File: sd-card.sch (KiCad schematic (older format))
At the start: 11 parts, among them J6 Micro_SD_Card_Det, U8 SN74AHC1G125DBVR

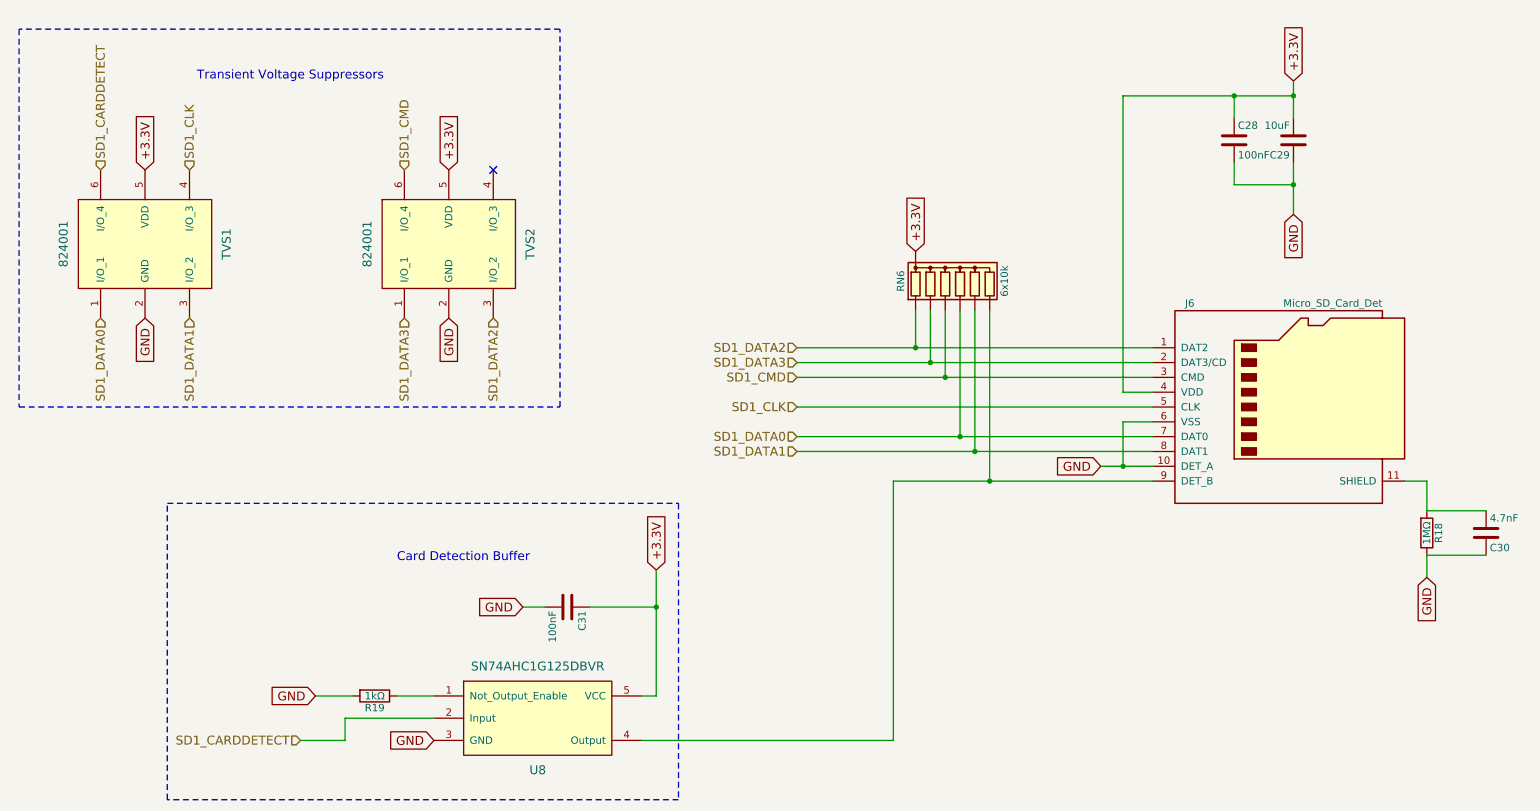
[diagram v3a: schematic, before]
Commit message: I have verified the schematic a second time (except the so-dimm), and I have selected all of the components with links and footprint. I need to verify the schematic a third time and root
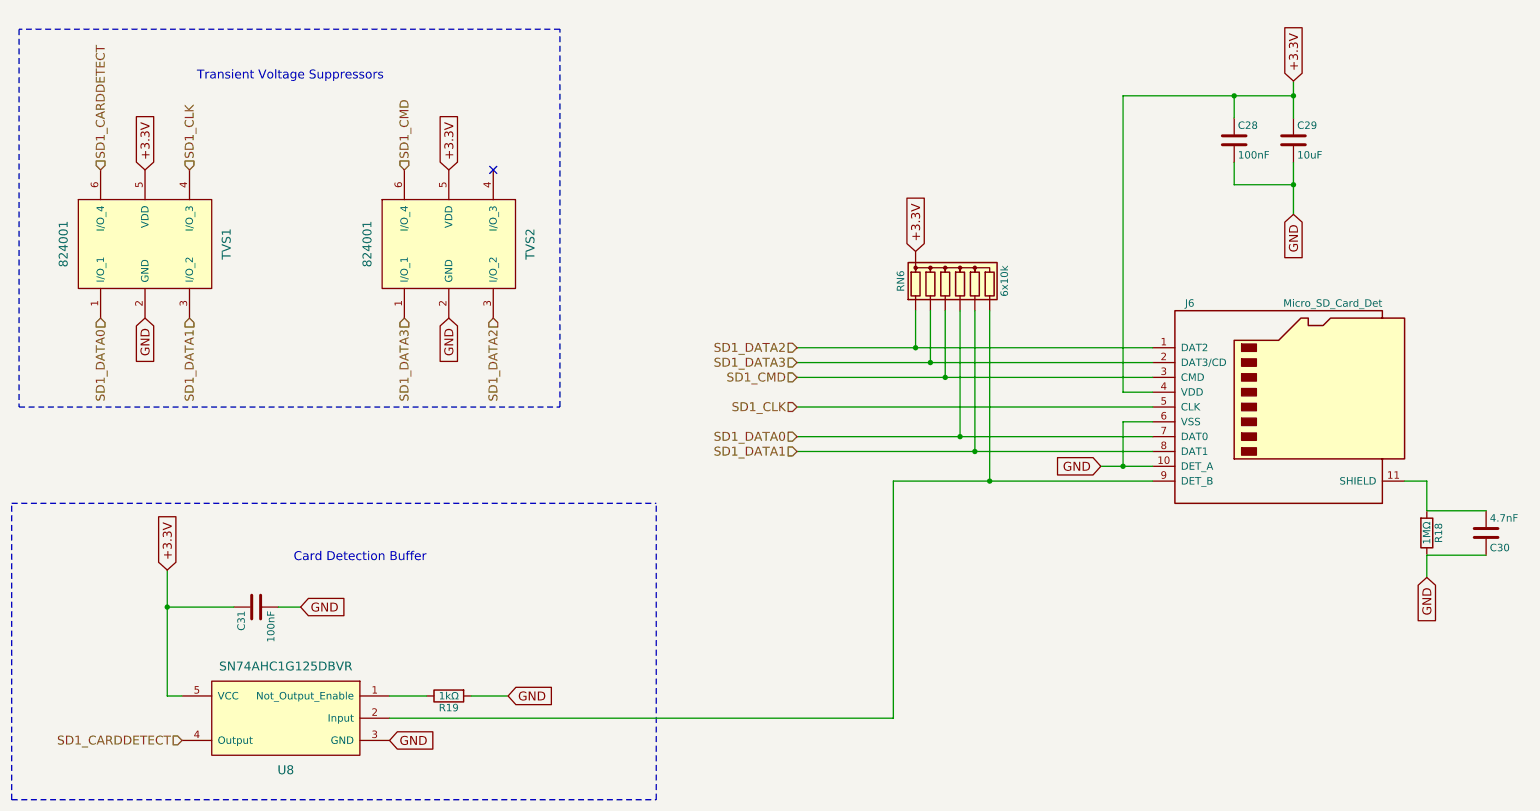
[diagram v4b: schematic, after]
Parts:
- RN6: footprint Resistors_THT:R_Array_SIP7 -> water:YC158-Yageo-Handsoldering
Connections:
- net +3.3V: now also C29.1; no longer C29.2
- net GND: now also C29.2; no longer C29.1
- net SD1_CARDDETECT: now also U8.4 (Output); no longer U8.2 (Input)
- net at J6.9 (DET_B), RN6.7 (R6): now also U8.2 (Input); no longer U8.4 (Output)
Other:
- moved on the sheet: C31, R19, U8
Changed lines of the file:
@@
 Text HLabel 6250 3300 0    60   Input ~ 0
 SD1_CLK
-Text HLabel 2900 5550 0    60   Input ~ 0
+Text HLabel 2100 5550 0    60   Input ~ 0
 SD1_CARDDETECT
 Text GLabel 7050 2250 1    60   Input ~ 0
@@
 F 0 "RN6" V 6950 2450 50  0000 C CNN
 F 1 "6x10k" V 7650 2450 50  0000 C CNN
-F 2 "Resistors_THT:R_Array_SIP7" V 7725 2450 50  0001 C CNN
-F 3 "http://hu.farnell.com/bourns/cay17-103jalf/resistor-n-w-8res-10kohm-5-smd/dp/2321752" H 7350 2450 50  0001 C CNN
+F 2 "water:YC158-Yageo-Handsoldering" V 7725 2450 50  0001 C CNN
+F 3 "http://hu.farnell.com/yageo-phycomp/yc158tjr-0710kl/resistor-array-8-10k-0-05-smd/dp/9236236" H 7350 2450 50  0001 C CNN
 	1    7350 2450
 	1    0    0    -1
@@
 L SN74AHC1G125DBVR U8
 U 1 1 59A18CB9
-P 4450 5100
-F 0 "U8" H 4500 4450 60  0000 C CNN
-F 1 "SN74AHC1G125DBVR" H 4500 5150 60  0000 C CNN
-F 2 "Housings_SOT-23_SOT-143_TSOT-6:SOT-23-5" H 4450 5100 60  0001 C CNN
-F 3 "hu.farnell.com/texas-instruments/sn74ahc1g125dbvt/ic-sm-logic-74ahc1g-buffer/dp/1607808" H 4450 5100 60  0001 C CNN
-	1    4450 5100
-	1    0    0    -1
+P 2850 5100
+F 0 "U8" H 2900 4450 60  0000 C CNN
+F 1 "SN74AHC1G125DBVR" H 2900 5150 60  0000 C CNN
+F 2 "Housings_SOT-23_SOT-143_TSOT-6:SOT-23-5" H 2850 5100 60  0001 C CNN
+F 3 "hu.farnell.com/texas-instruments/sn74ahc1g125dbvt/ic-sm-logic-74ahc1g-buffer/dp/1607808" H 2850 5100 60  0001 C CNN
+	1    2850 5100
+	-1   0    0    -1
 $EndComp
 Text Notes 2200 1100 0    60   ~ 0
@@
 Wire Notes Line
 	4650 750  1000 750
-Text GLabel 3800 5550 0    60   Input ~ 0
-GND
-Text GLabel 5300 4400 1    60   Input ~ 0
-+3.3V
-Text GLabel 3000 5250 0    60   Input ~ 0
-GND
-Wire Wire Line
-	3000 5250 3250 5250
-Wire Wire Line
-	3550 5250 3800 5250
-Wire Wire Line
-	3800 5400 3200 5400
-Wire Wire Line
-	3200 5400 3200 5550
-Wire Wire Line
-	3200 5550 2900 5550
-Wire Wire Line
-	5200 5550 6900 5550
-Wire Wire Line
-	5300 4400 5300 5250
-Wire Wire Line
-	5300 5250 5200 5250
-Text GLabel 4400 4650 0    60   Input ~ 0
-GND
-Wire Wire Line
-	5300 4650 4850 4650
-Wire Wire Line
-	4550 4650 4400 4650
-Connection ~ 5300 4650
-Wire Wire Line
-	6900 5550 6900 3800
+Text GLabel 3500 5550 2    60   Input ~ 0
+GND
+Text GLabel 2000 4400 1    60   Input ~ 0
++3.3V
+Text GLabel 4300 5250 2    60   Input ~ 0
+GND
+Wire Wire Line
+	4300 5250 4050 5250
+Wire Wire Line
+	3750 5250 3500 5250
+Wire Wire Line
+	3500 5400 6900 5400
+Wire Wire Line
+	2000 4400 2000 5250
+Wire Wire Line
+	2000 5250 2100 5250
+Text GLabel 2900 4650 2    60   Input ~ 0
+GND
+Wire Wire Line
+	2000 4650 2450 4650
+Wire Wire Line
+	2750 4650 2900 4650
+Connection ~ 2000 4650
 Wire Wire Line
 	6900 3800 8650 3800
-Text Notes 3550 4350 0    60   ~ 0
+Text Notes 3750 4350 2    60   ~ 0
 Card Detection Buffer
 Wire Notes Line
-	2000 3950 5450 3950
-Wire Notes Line
-	5450 3950 5450 5950
-Wire Notes Line
-	5450 5950 2000 5950
-Wire Notes Line
-	2000 5950 2000 3950
+	950  3950 5300 3950
+Wire Notes Line
+	950  5950 5300 5950
+Wire Notes Line
+	5300 5950 5300 3950
 Text GLabel 8300 3700 0    60   Input ~ 0
 GND
@@
 L R R19
 U 1 1 59A82701
-P 3400 5250
-F 0 "R19" V 3480 5250 50  0000 C CNN
-F 1 "1kΩ" V 3400 5250 50  0000 C CNN
-F 2 "Resistors_SMD:R_0603_HandSoldering" V 3330 5250 30  0001 C CNN
-F 3 "hu.farnell.com/multicomp/mcmr06x1001ftl/res-ceramic-1k-1-0-1w-0603/dp/2073348" H 3400 5250 30  0001 C CNN
-	1    3400 5250
-	0    1    1    0
+P 3900 5250
+F 0 "R19" V 3980 5250 50  0000 C CNN
+F 1 "1kΩ" V 3900 5250 50  0000 C CNN
+F 2 "Resistors_SMD:R_0603_HandSoldering" V 3830 5250 30  0001 C CNN
+F 3 "hu.farnell.com/multicomp/mcmr06x1001ftl/res-ceramic-1k-1-0-1w-0603/dp/2073348" H 3900 5250 30  0001 C CNN
+	1    3900 5250
+	0    -1   1    0
 $EndComp
 $Comp
@@
 F 4 "http://hu.farnell.com/avx/06036d106mat2a/cap-mlcc-x5r-10uf-6-3v-0603/dp/1833804" H 9600 1500 60  0001 C CNN "avx"
 	1    9600 1500
-	-1   0    0    1
+	1    0    0    -1
 $EndComp
 $Comp
@@
 L C C31
 U 1 1 59A67859
-P 4700 4650
-F 0 "C31" H 4725 4750 50  0000 L CNN
-F 1 "100nF" H 4725 4550 50  0000 L CNN
-F 2 "Capacitors_SMD:C_0603_HandSoldering" H 4738 4500 30  0001 C CNN
-F 3 "hu.farnell.com/avx/06035c104kat2a/cap-mlcc-x7r-100nf-50v-0603/dp/1301804" H 4700 4650 60  0001 C CNN
-	1    4700 4650
-	0    1    1    0
+P 2600 4650
+F 0 "C31" H 2625 4750 50  0000 L CNN
+F 1 "100nF" H 2625 4550 50  0000 L CNN
+F 2 "Capacitors_SMD:C_0603_HandSoldering" H 2638 4500 30  0001 C CNN
+F 3 "hu.farnell.com/avx/06035c104kat2a/cap-mlcc-x7r-100nf-50v-0603/dp/1301804" H 2600 4650 60  0001 C CNN
+	1    2600 4650
+	0    -1   1    0
 $EndComp
 $Comp
@@
 $EndComp
 NoConn ~ 4200 1700
+Wire Notes Line
+	950  5950 950  3950
+Wire Wire Line
+	6900 5400 6900 3800
 $EndSCHEMATC

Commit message: part numbers generated;
pcb generation started
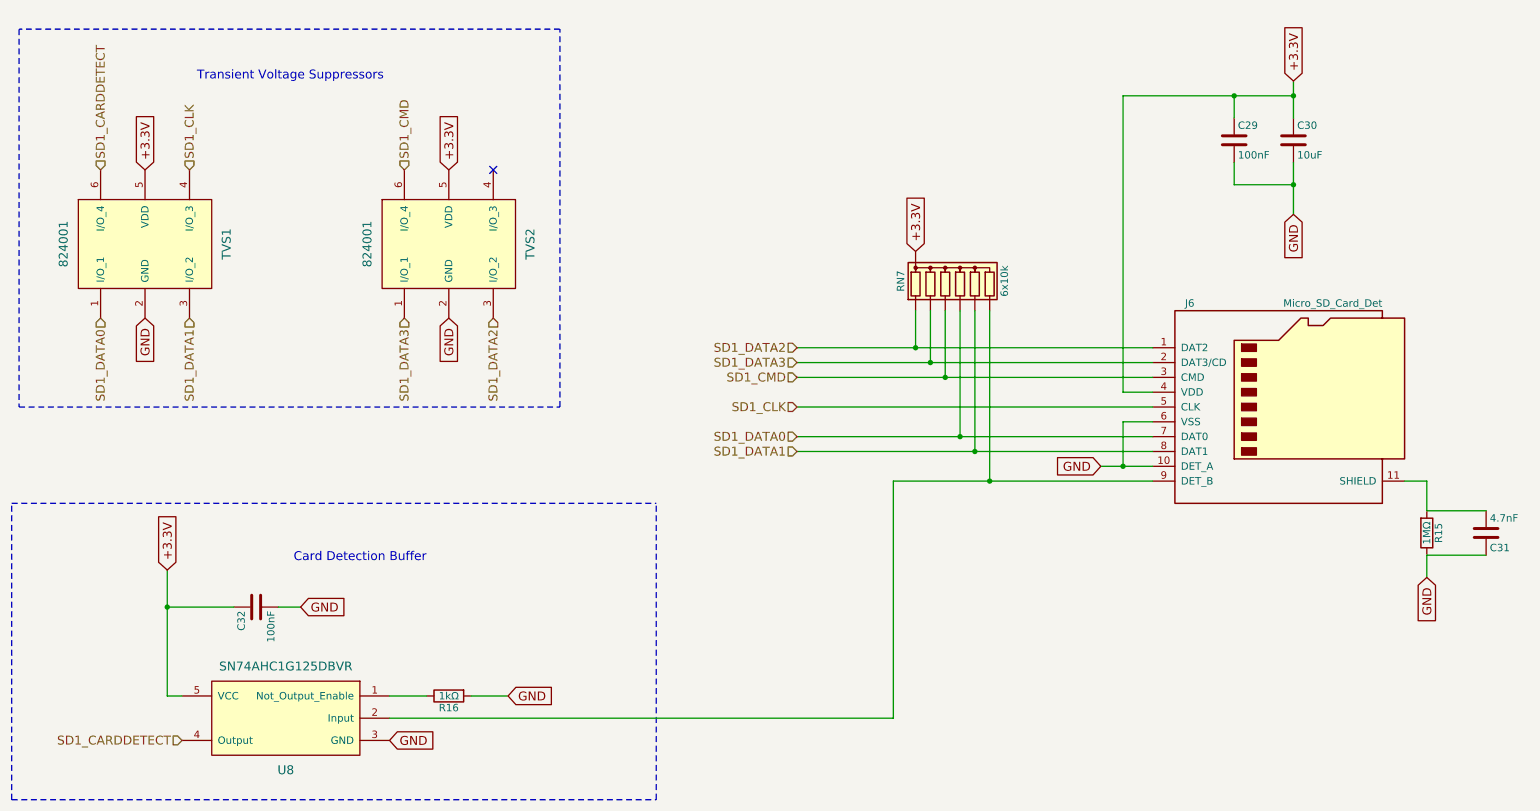
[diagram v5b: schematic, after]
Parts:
- renumbered C28 to C29, C29 to C30, C30 to C31, C31 to C32, R18 to R15, R19 to R16, RN6 to RN7
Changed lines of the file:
@@
 	6250 3600 8650 3600
 $Comp
-L R_Network06 RN6
+L R_Network06 RN7
 U 1 1 59A16EDB
 P 7350 2450
-F 0 "RN6" V 6950 2450 50  0000 C CNN
+F 0 "RN7" V 6950 2450 50  0000 C CNN
 F 1 "6x10k" V 7650 2450 50  0000 C CNN
 F 2 "water:YC158-Yageo-Handsoldering" V 7725 2450 50  0001 C CNN
@@
 	10500 3800 10350 3800
 $Comp
-L R R19
+L R R16
 U 1 1 59A82701
 P 3900 5250
-F 0 "R19" V 3980 5250 50  0000 C CNN
+F 0 "R16" V 3980 5250 50  0000 C CNN
 F 1 "1kΩ" V 3900 5250 50  0000 C CNN
 F 2 "Resistors_SMD:R_0603_HandSoldering" V 3830 5250 30  0001 C CNN
@@
 $EndComp
 $Comp
-L C C29
+L C C30
 U 1 1 59A66C23
 P 9600 1500
-F 0 "C29" H 9625 1600 50  0000 L CNN
+F 0 "C30" H 9625 1600 50  0000 L CNN
 F 1 "10uF" H 9625 1400 50  0000 L CNN
 F 2 "Capacitors_SMD:C_0603_HandSoldering" H 9638 1350 30  0001 C CNN
@@
 $EndComp
 $Comp
-L C C28
+L C C29
 U 1 1 59A672EC
 P 9200 1500
-F 0 "C28" H 9225 1600 50  0000 L CNN
+F 0 "C29" H 9225 1600 50  0000 L CNN
 F 1 "100nF" H 9225 1400 50  0000 L CNN
 F 2 "Capacitors_SMD:C_0603_HandSoldering" H 9238 1350 30  0001 C CNN
@@
 $EndComp
 $Comp
-L C C31
+L C C32
 U 1 1 59A67859
 P 2600 4650
-F 0 "C31" H 2625 4750 50  0000 L CNN
+F 0 "C32" H 2625 4750 50  0000 L CNN
 F 1 "100nF" H 2625 4550 50  0000 L CNN
 F 2 "Capacitors_SMD:C_0603_HandSoldering" H 2638 4500 30  0001 C CNN
@@
 $EndComp
 $Comp
-L R R18
+L R R15
 U 1 1 59A6A008
 P 10500 4150
-F 0 "R18" V 10580 4150 50  0000 C CNN
+F 0 "R15" V 10580 4150 50  0000 C CNN
 F 1 "1MΩ" V 10500 4150 50  0000 C CNN
 F 2 "Resistors_SMD:R_0603_HandSoldering" V 10430 4150 50  0001 C CNN
@@
 $EndComp
 $Comp
-L C C30
+L C C31
 U 1 1 59A6A959
 P 10900 4150
-F 0 "C30" H 10925 4250 50  0000 L CNN
+F 0 "C31" H 10925 4250 50  0000 L CNN
 F 1 "4.7nF" H 10925 4050 50  0000 L CNN
 F 2 "Capacitors_SMD:C_0603_HandSoldering" H 10938 4000 50  0001 C CNN

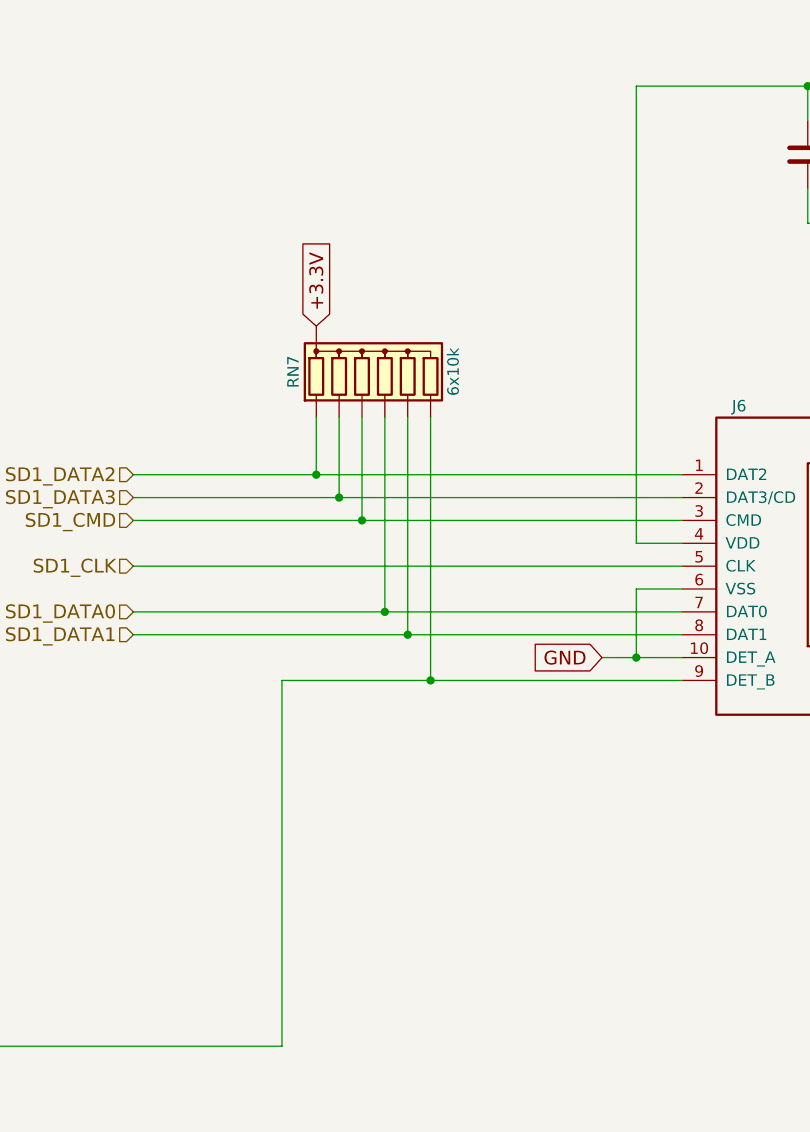
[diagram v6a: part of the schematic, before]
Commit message: I have replaced the 8xresistors to 4resistors because the distance between the pads was not big enough for the 3um copper layers
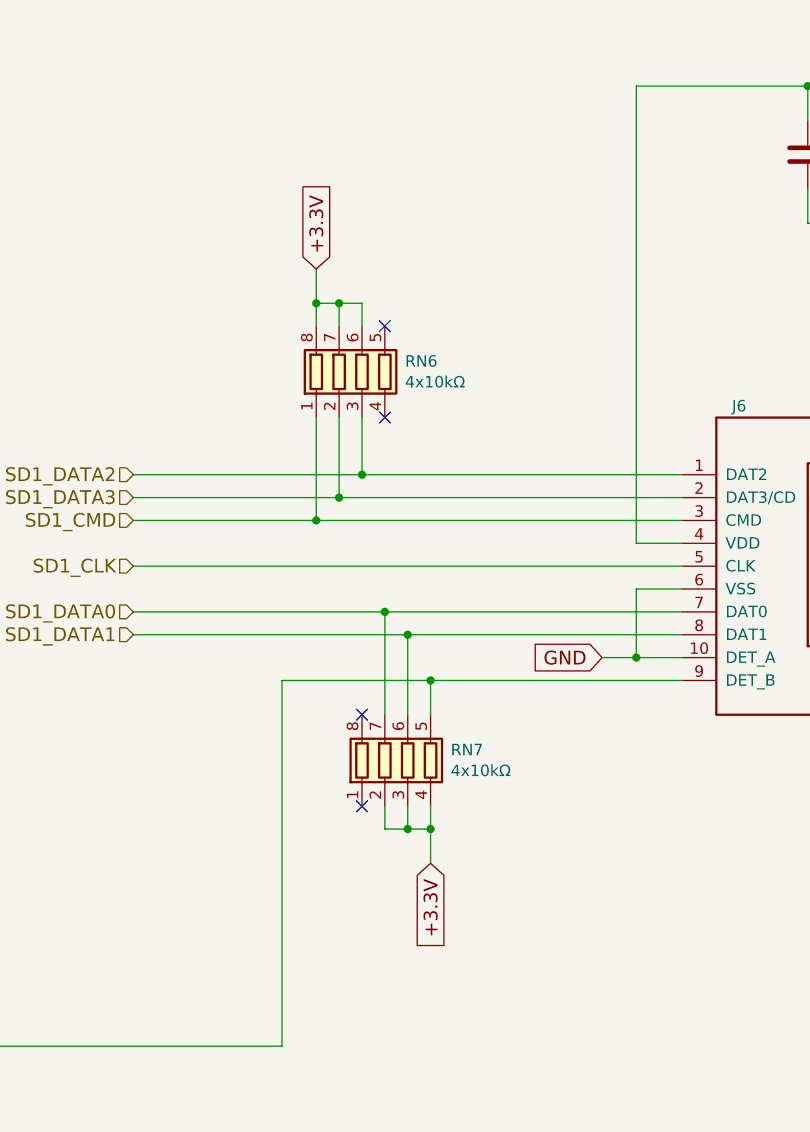
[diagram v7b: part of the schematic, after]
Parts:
- removed RN7: 6x10k, water:YC158-Yageo-Handsoldering, symbol R_Network06
- added RN6, RN7: 4x10kΩ, kilibs:YC164-Yageo-Handsoldering, symbol R_Pack04
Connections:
- net +3.3V: now also RN6.6 (R3.2), RN6.7 (R2.2), RN6.8 (R1.2), RN7.2 (R2.1), RN7.3 (R3.1), RN7.4 (R4.1)
- net SD1_CMD: now also RN6.1 (R1.1)
- net SD1_DATA0: now also RN7.7 (R2.2)
- net SD1_DATA1: now also RN7.6 (R3.2)
- net SD1_DATA2: now also RN6.3 (R3.1)
- net SD1_DATA3: now also RN6.2 (R2.1)
- net at J6.9 (DET_B), U8.2 (Input): now also RN7.5 (R4.2)
- no-connect marks 1 -> 5
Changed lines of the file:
@@
 Text HLabel 2100 5550 0    60   Input ~ 0
 SD1_CARDDETECT
-Text GLabel 7050 2250 1    60   Input ~ 0
+Text GLabel 7050 2000 1    60   Input ~ 0
 +3.3V
 Wire Wire Line
@@
 Wire Wire Line
 	6250 3500 8650 3500
-Wire Wire Line
-	6250 3600 8650 3600
-$Comp
-L R_Network06 RN7
-U 1 1 59A16EDB
-P 7350 2450
-F 0 "RN7" V 6950 2450 50  0000 C CNN
-F 1 "6x10k" V 7650 2450 50  0000 C CNN
-F 2 "water:YC158-Yageo-Handsoldering" V 7725 2450 50  0001 C CNN
-F 3 "http://hu.farnell.com/yageo-phycomp/yc158tjr-0710kl/resistor-array-8-10k-0-05-smd/dp/9236236" H 7350 2450 50  0001 C CNN
-	1    7350 2450
-	1    0    0    -1
-$EndComp
-Wire Wire Line
-	7050 2650 7050 2900
-Connection ~ 7050 2900
-Wire Wire Line
-	7150 2650 7150 3000
-Connection ~ 7150 3000
-Wire Wire Line
-	7250 2650 7250 3100
-Connection ~ 7250 3100
-Wire Wire Line
-	7350 2650 7350 3500
-Connection ~ 7350 3500
-Wire Wire Line
-	7450 2650 7450 3600
-Connection ~ 7450 3600
-Wire Wire Line
-	7550 2650 7550 3800
-Connection ~ 7550 3800
 Text GLabel 9600 1100 1    60   Input ~ 0
 +3.3V
@@
 Wire Wire Line
 	6900 5400 6900 3800
+$Comp
+L R_Pack04 RN6
+U 1 1 59B15571
+P 7250 2450
+F 0 "RN6" H 7438 2496 50  0000 L CNN
+F 1 "4x10kΩ" H 7438 2405 50  0000 L CNN
+F 2 "kilibs:YC164-Yageo-Handsoldering" V 7525 2450 50  0001 C CNN
+F 3 "http://hu.farnell.com/yageo-phycomp/yc164-jr-0710kl/resistor-array-arv241-1206-10k/dp/9234560" H 7250 2450 50  0001 C CNN
+	1    7250 2450
+	1    0    0    -1
+$EndComp
+Wire Wire Line
+	7050 2250 7050 2000
+Wire Wire Line
+	7050 2150 7250 2150
+Wire Wire Line
+	7150 2150 7150 2250
+Connection ~ 7050 2150
+Wire Wire Line
+	7250 2150 7250 2250
+Connection ~ 7150 2150
+Text GLabel 7550 4600 3    60   Input ~ 0
++3.3V
+Wire Wire Line
+	7550 4600 7550 4350
+Wire Wire Line
+	7350 4450 7550 4450
+Wire Wire Line
+	7450 4450 7450 4350
+Connection ~ 7550 4450
+Wire Wire Line
+	7350 4450 7350 4350
+Connection ~ 7450 4450
+$Comp
+L R_Pack04 RN7
+U 1 1 59B16EB8
+P 7450 4150
+F 0 "RN7" H 7638 4196 50  0000 L CNN
+F 1 "4x10kΩ" H 7638 4105 50  0000 L CNN
+F 2 "kilibs:YC164-Yageo-Handsoldering" V 7725 4150 50  0001 C CNN
+F 3 "http://hu.farnell.com/yageo-phycomp/yc164-jr-0710kl/resistor-array-arv241-1206-10k/dp/9234560" H 7450 4150 50  0001 C CNN
+	1    7450 4150
+	1    0    0    -1
+$EndComp
+NoConn ~ 7250 4350
+NoConn ~ 7250 3950
+NoConn ~ 7350 2650
+NoConn ~ 7350 2250
+Wire Wire Line
+	7050 2650 7050 3100
+Connection ~ 7050 3100
+Wire Wire Line
+	7150 2650 7150 3000
+Connection ~ 7150 3000
+Wire Wire Line
+	7250 2650 7250 2900
+Connection ~ 7250 2900
+Wire Wire Line
+	6250 3600 8650 3600
+Wire Wire Line
+	7350 3950 7350 3500
+Connection ~ 7350 3500
+Wire Wire Line
+	7450 3950 7450 3600
+Connection ~ 7450 3600
+Wire Wire Line
+	7550 3950 7550 3800
+Connection ~ 7550 3800
 $EndSCHEMATC
